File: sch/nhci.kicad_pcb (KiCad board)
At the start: 4 copper layers, 64 parts, among them IC1 74LVC8T245RHLRG4, IC2 74LVC8T245RHLRG4, IC3 74LVC8T245RHLRG4, IC4 74LVC8T245RHLRG4, IC5 74LVC8T245RHLRG4, IC6 MAX3421EEHJ+, IC7 LT3030IFE#TRPBF, SW1 SW_Push_Open, U1 PCMCIA_BOARD, U2 iCE40-HX8K-CT256, U3 N25Q032A13EF440F, U4 LM3526M-H, Y1 ECS-5032MV-120-BM-TR

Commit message: Route forgotten
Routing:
- net +3V3: track 120.7 -> 129.8 mm, vias 25 -> 27
- net Net-(C25-Pad1): track 0.00 -> 1.70 mm
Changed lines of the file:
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@@
     (thickness 1.6)
     (drawings 0)
-    (tracks 1035)
+    (tracks 1046)
     (zones 0)
     (modules 64)
@@
   (segment (start 77.296999 136.224999) (end 72.644 131.572) (width 0.2) (layer In2.Cu) (net 102))
   (segment (start 69.85 137.5365) (end 69.85 137.414) (width 0.2) (layer F.Cu) (net 102))
-  (segment (start 68.052 139.3345) (end 69.85 137.5365) (width 0.2) (layer F.Cu) (net 102))
   (segment (start 68.052 140.272) (end 68.052 139.3345) (width 0.2) (layer F.Cu) (net 102))
   (segment (start 68.052 148.085) (end 68.052 146.748) (width 0.2) (layer F.Cu) (net 102))
@@
   (segment (start 69.85 137.414) (end 69.85 134.366) (width 0.2) (layer F.Cu) (net 102))
   (segment (start 69.85 134.366) (end 72.644 131.572) (width 0.2) (layer F.Cu) (net 102))
+  (segment (start 68.052 145.137962) (end 67.31 144.395962) (width 0.2) (layer F.Cu) (net 102))
+  (segment (start 68.052 146.748) (end 68.052 145.137962) (width 0.2) (layer F.Cu) (net 102))
+  (via (at 67.30602 144.396933) (size 0.4) (drill 0.2) (layers F.Cu B.Cu) (net 102))
+  (segment (start 67.31 144.395962) (end 67.306991 144.395962) (width 0.2) (layer F.Cu) (net 102))
+  (segment (start 67.306991 144.395962) (end 67.30602 144.396933) (width 0.2) (layer F.Cu) (net 102))
+  (segment (start 67.30602 140.08048) (end 68.76825 138.61825) (width 0.2) (layer B.Cu) (net 102))
+  (segment (start 67.30602 144.396933) (end 67.30602 140.08048) (width 0.2) (layer B.Cu) (net 102))
+  (segment (start 68.052 139.3345) (end 68.76825 138.61825) (width 0.2) (layer F.Cu) (net 102))
+  (via (at 68.76825 138.61825) (size 0.4) (drill 0.2) (layers F.Cu B.Cu) (net 102))
+  (segment (start 68.76825 138.61825) (end 69.85 137.5365) (width 0.2) (layer F.Cu) (net 102))
   (segment (start 80.518001 106.131998) (end 78.780002 106.131998) (width 0.2) (layer F.Cu) (net 103))
   (segment (start 81.046 107.316) (end 81.046 106.659997) (width 0.2) (layer F.Cu) (net 103))
@@
   (segment (start 85.575 134.5) (end 85.441 134.366) (width 0.2) (layer F.Cu) (net 336))
   (segment (start 85.575 135.89) (end 85.575 134.5) (width 0.2) (layer F.Cu) (net 336))
+  (segment (start 81.037 132.115) (end 81.026 132.126) (width 0.2) (layer F.Cu) (net 337))
+  (segment (start 81.037 130.433) (end 81.037 132.115) (width 0.2) (layer F.Cu) (net 337))
   (segment (start 85.598 130.444) (end 85.587 130.433) (width 0.2) (layer F.Cu) (net 338))
   (segment (start 85.598 131.849) (end 85.598 130.444) (width 0.2) (layer F.Cu) (net 338))

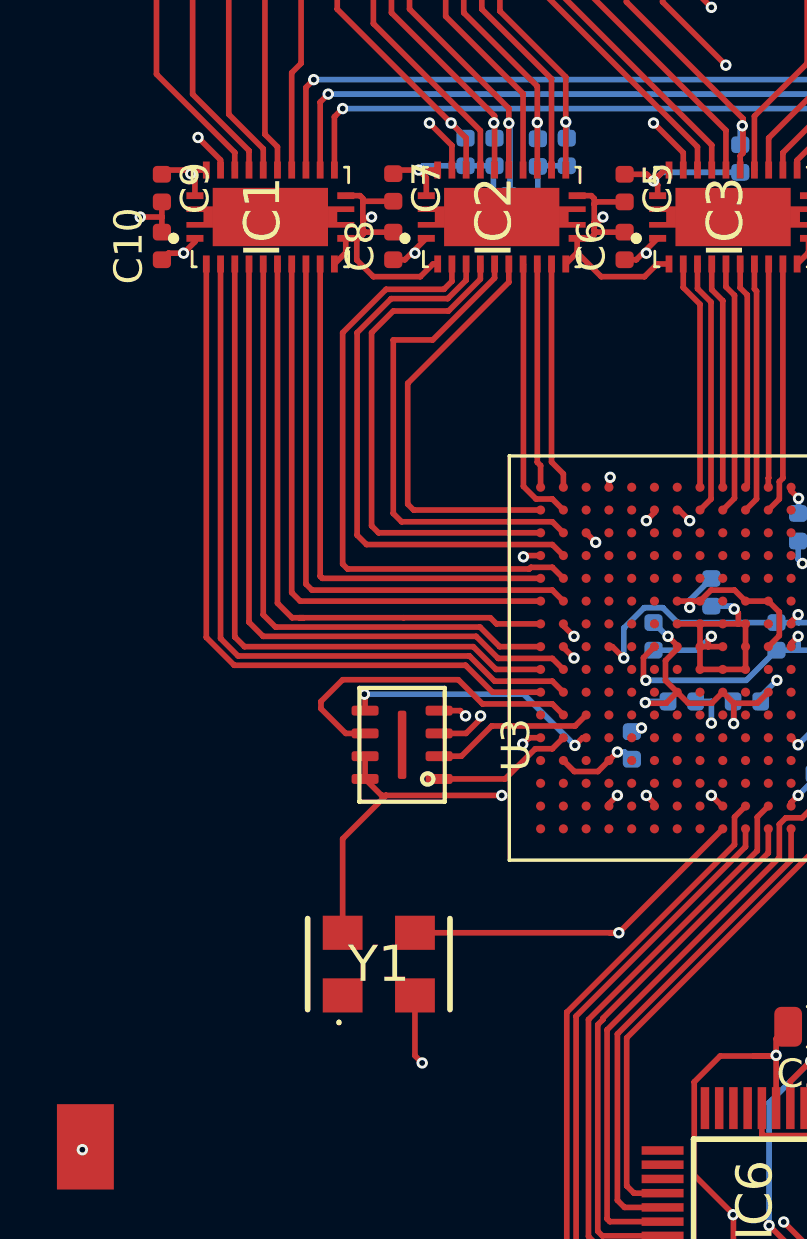
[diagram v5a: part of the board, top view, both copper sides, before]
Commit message: Add programming connector
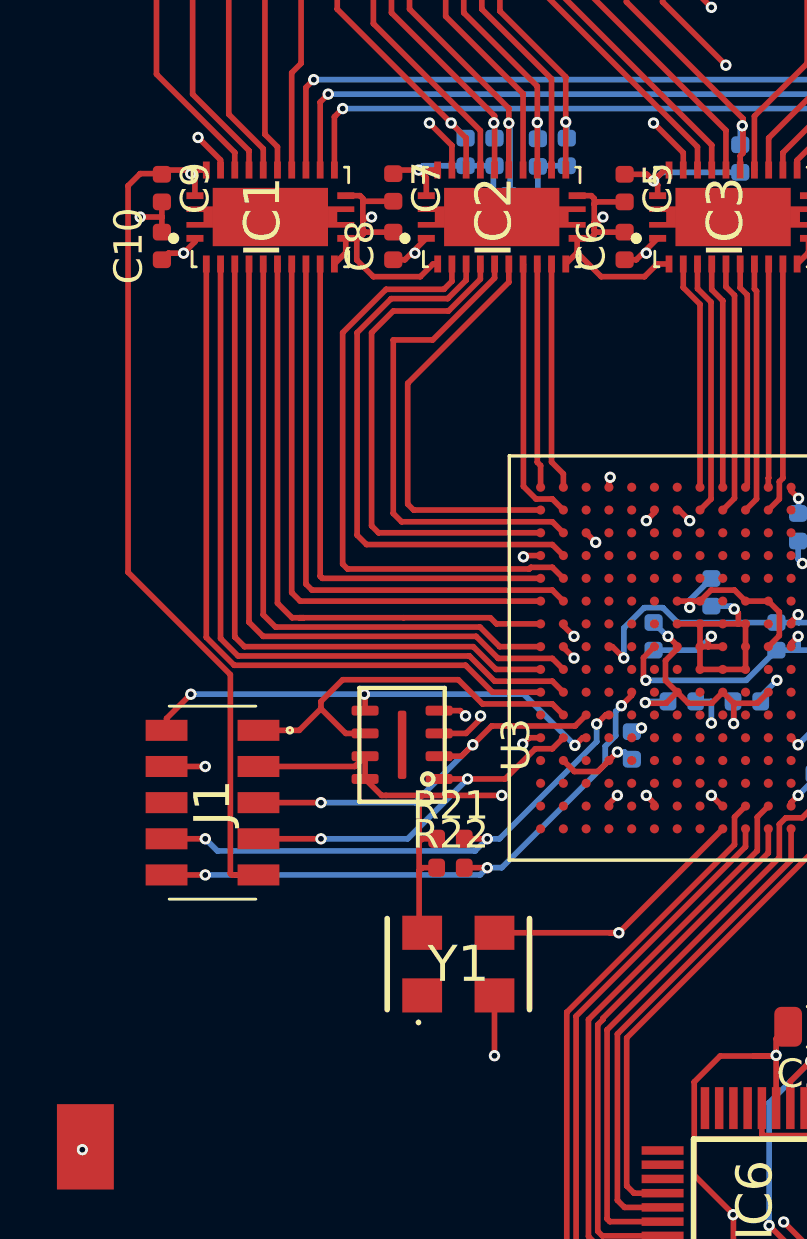
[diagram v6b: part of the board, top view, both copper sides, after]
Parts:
- added J1: CLP-105-02-F-D, CLP-105-02-F-D:CLP-105-02-XXX-D, F.Cu at (47.8, 129.5)
- added R21: R, Resistor_SMD:R_0402_1005Metric, F.Cu at (56.1, 130.8)
- added R22: R, Resistor_SMD:R_0402_1005Metric, F.Cu at (56.1, 131.8)
- moved Y1 2.79 mm to (56.4, 135.2)
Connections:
- U2 pad M10: Net-(U2-PadM10) -> CDONE
- U2 pad N11: Net-(U2-PadN11) -> CRESET
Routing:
- net +5V: track 129.8 -> 157.8 mm
- net CDONE: track 0.00 -> 20.7 mm, vias 0 -> 3
- net CRESET: track 0.00 -> 18.9 mm, vias 0 -> 3
- net Net-(J1-Pad5): track 5.77 -> 14.1 mm, vias 0 -> 2
- net Net-(J1-Pad7): track 4.97 -> 13.2 mm, vias 0 -> 2
- net Net-(J1-Pad2): track 9.24 -> 17.0 mm, vias 2 -> 3
- net +3V3: track 129.8 -> 134.4 mm
- net 12MHz: track 27.9 -> 25.1 mm
- net Net-(J1-Pad1): track 11.5 -> 14.0 mm
- net GND: track 140.1 -> 141.1 mm, vias 37 -> 38

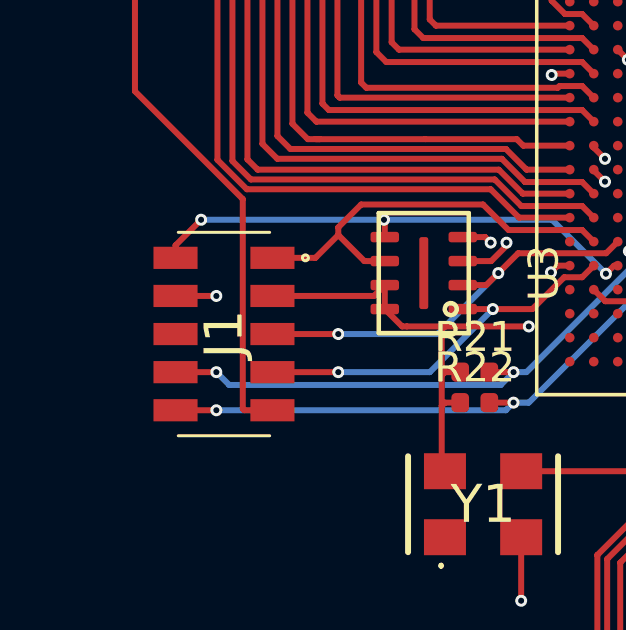
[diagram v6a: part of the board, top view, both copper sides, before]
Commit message: Add missing route
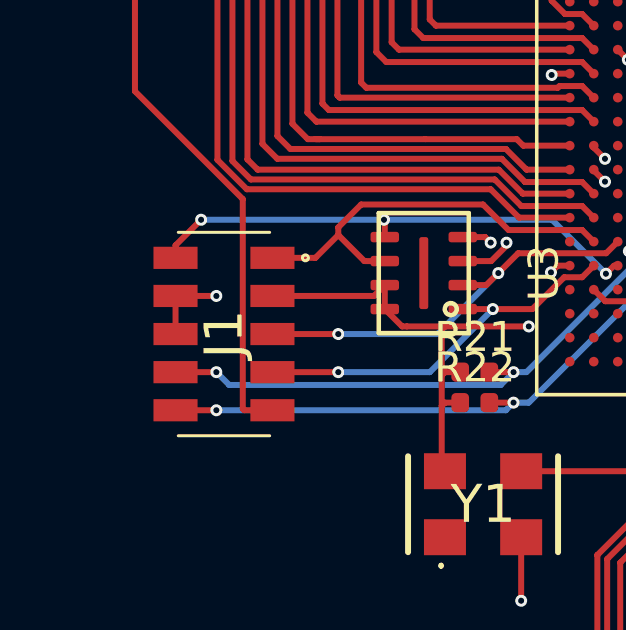
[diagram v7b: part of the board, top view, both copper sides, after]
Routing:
- net GND: track 141.1 -> 142.4 mm
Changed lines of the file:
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@@
     (thickness 1.6)
     (drawings 0)
-    (tracks 1110)
+    (tracks 1111)
     (zones 0)
     (modules 67)
@@
   (via (at 47.498 128.27) (size 0.4) (drill 0.2) (layers F.Cu B.Cu) (net 69))
   (segment (start 46.137 128.27) (end 47.498 128.27) (width 0.2) (layer F.Cu) (net 69))
+  (segment (start 46.137 129.54) (end 46.137 128.27) (width 0.2) (layer F.Cu) (net 69))
   (segment (start 49.034 106.634302) (end 49.034 107.316) (width 0.2) (layer F.Cu) (net 70))
   (segment (start 47.0535 104.653802) (end 49.034 106.634302) (width 0.2) (layer F.Cu) (net 70))

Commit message: Add proper value of resistors
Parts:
- R21, R22: value R -> 10k
